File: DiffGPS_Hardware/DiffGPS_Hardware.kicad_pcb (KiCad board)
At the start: 2 copper layers, 87.6 x 72.1 mm, 17 parts, among them U1 Raspberry_Pi, U2 TSR_1-2450

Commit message: Finished Layout
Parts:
- removed the G*** at (116.8, 109.2)
- removed the G*** at (64.5, 73.2)
- added C1: 10uF, Capacitor_SMD:C_0603_1608Metric_Pad1.08x0.95mm_HandSolder, F.Cu at (63.4, 59.2)
- added C2: 10uF, Capacitor_SMD:C_0603_1608Metric_Pad1.08x0.95mm_HandSolder, F.Cu at (63.4, 61.4)
- added H4: MountingHole, MRDT_Drill_Holes:4_40_Hole_Corner, F.Cu at (50.9, 81.5)
- R1: value 1k -> 3k
- R3: value 120 -> 100
- U2: value TSR_1-2450 -> OKI; footprint MRDT_Devices:TSR_1-2433 -> MRDT_Devices:OKI_Horizontal
- moved G*** 3.97 mm to (111.3, 73.7)
- moved U2 2.05 mm to (68.6, 59.2)
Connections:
- net +12V renamed VCC
- net GPS_RX1 renamed D1
- net GPS_TX1 renamed D0
- net GPS_TX2 renamed D2
- A1 pad 10: unconnected-(A1-Pad10) -> A1
- A1 pad 11: unconnected-(A1-Pad11) -> A2
- A1 pad 12: unconnected-(A1-Pad12) -> A3
- A1 pad 13: unconnected-(A1-Pad13) -> A4
- A1 pad 14: unconnected-(A1-Pad14) -> A5
- A1 pad 18: unconnected-(A1-Pad18) -> D3
- A1 pad 19: unconnected-(A1-Pad19) -> D4
- A1 pad 20: unconnected-(A1-Pad20) -> D5
- A1 pad 21: unconnected-(A1-Pad21) -> D6
- A1 pad 22: unconnected-(A1-Pad22) -> D7
- A1 pad 23: GPS_RX2 -> D8
- A1 pad 24: unconnected-(A1-Pad24) -> D9
- A1 pad 25: unconnected-(A1-Pad25) -> D10
- A1 pad 26: unconnected-(A1-Pad26) -> D11
- A1 pad 27: unconnected-(A1-Pad27) -> D12
- A1 pad 28: unconnected-(A1-Pad28) -> D13
- A1 pad 9: unconnected-(A1-Pad9) -> A0
- U1 pad 12: unconnected-(U1-Pad12) -> D3
- U1 pad 13: unconnected-(U1-Pad13) -> D5
- U1 pad 15: unconnected-(U1-Pad15) -> D6
- U1 pad 16: GPS_RX2 -> D7
- U1 pad 19: unconnected-(U1-Pad19) -> D11
- U1 pad 21: unconnected-(U1-Pad21) -> D12
- U1 pad 22: unconnected-(U1-Pad22) -> D9
- U1 pad 23: unconnected-(U1-Pad23) -> D13
- U1 pad 24: unconnected-(U1-Pad24) -> D10
- U1 pad 26: unconnected-(U1-Pad26) -> D4
- U1 pad 29: unconnected-(U1-Pad29) -> A1
- U1 pad 3: unconnected-(U1-Pad3) -> A4
- U1 pad 31: unconnected-(U1-Pad31) -> A2
- U1 pad 32: unconnected-(U1-Pad32) -> A3
- U1 pad 5: unconnected-(U1-Pad5) -> A5
- U1 pad 7: unconnected-(U1-Pad7) -> A0
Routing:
- net D4: track 0.00 -> 86.1 mm, vias 0 -> 2
- net D11: track 0.00 -> 70.0 mm, vias 0 -> 2
- net D9: track 0.00 -> 68.2 mm
- net D3: track 0.00 -> 64.3 mm, vias 0 -> 2
- net D13: track 0.00 -> 62.7 mm
- net D12: track 0.00 -> 61.1 mm, vias 0 -> 2
- net GPS_RX2: track 60.8 -> 0.00 mm
- net D7: track 0.00 -> 60.1 mm
- net D10: track 0.00 -> 59.2 mm
- net D6: track 0.00 -> 55.9 mm
- net D5: track 0.00 -> 55.8 mm
- net A3: track 0.00 -> 39.6 mm, vias 0 -> 1
- net A2: track 0.00 -> 34.3 mm, vias 0 -> 1
- net A1: track 0.00 -> 30.5 mm, vias 0 -> 2
- net A0: track 0.00 -> 13.2 mm, vias 0 -> 2
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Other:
- board text added: "Differential GPS Breakout Board, Rev1 Mars Rover Design Team Missouri S&T, 2024 Will Grove, Natasha Cox"
- board text removed: "Differential GPS Breakout Board, Rev1 Mars Rover Design Team Missouri S&T, 2023 Grant Brinker"

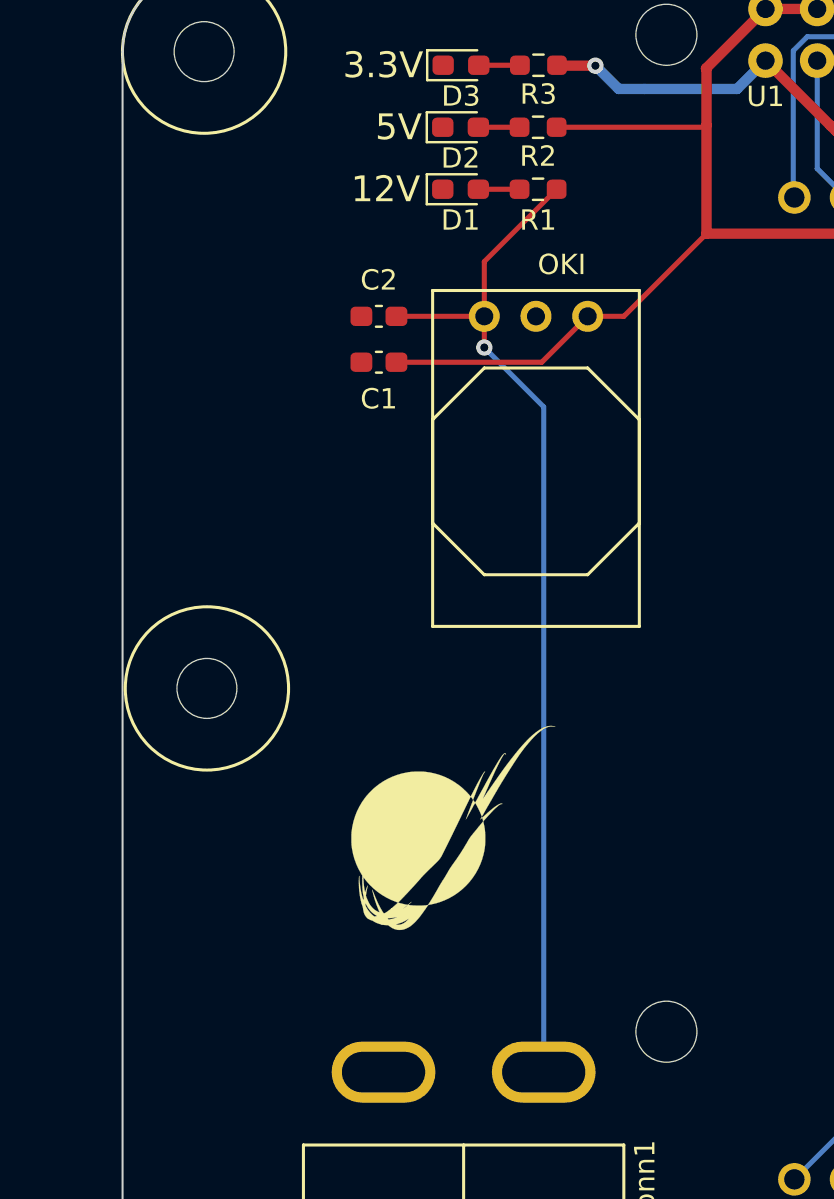
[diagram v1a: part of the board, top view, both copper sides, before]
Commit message: Fixed some stuff, changed trace width
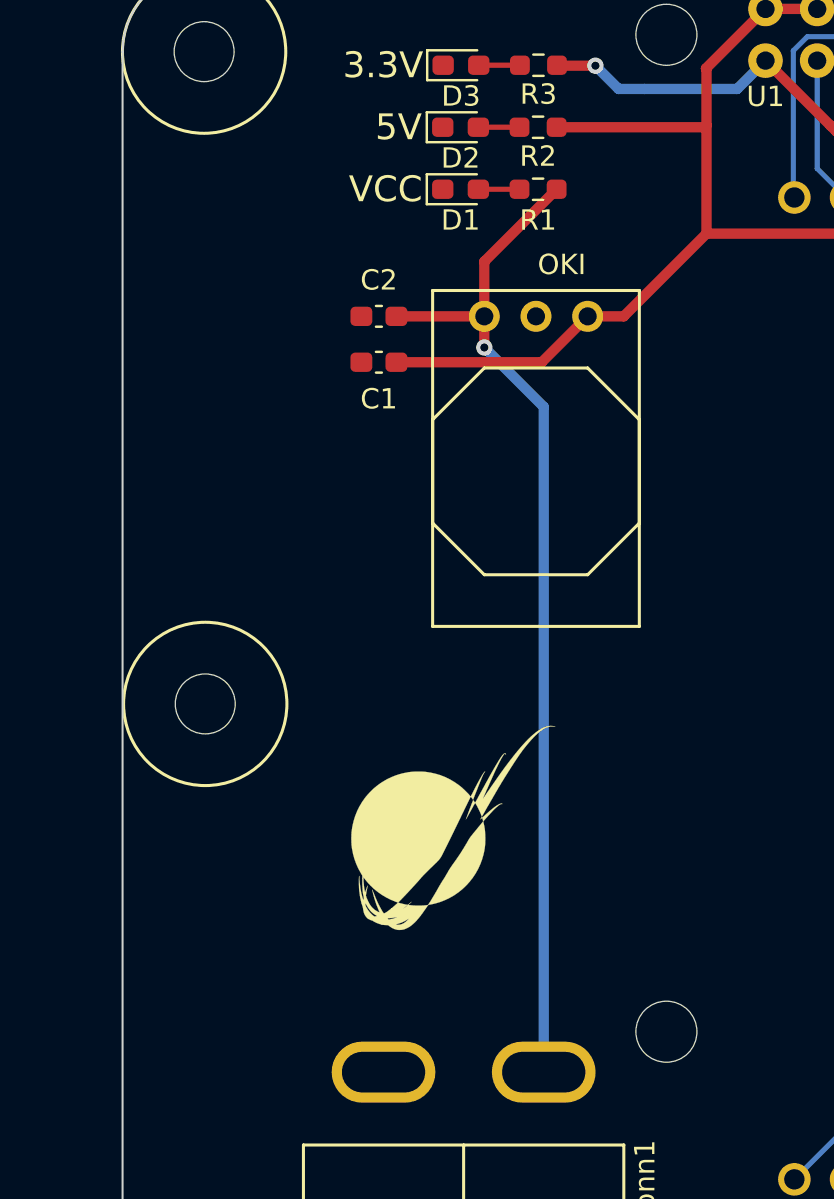
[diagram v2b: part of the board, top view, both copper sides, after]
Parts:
- moved H4 0.77 mm to (50.9, 82.2)
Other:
- board text added: "VCC"
- board text removed: "12V"
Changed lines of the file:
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@@
   )
   (footprint "MRDT_Drill_Holes:4_40_Hole_Corner" (layer "F.Cu")
-    (at 50.9383 81.47812)
+    (at 50.85588 82.24012)
     (property "Sheetfile" "DiffGPS_Hardware.kicad_sch")
     (property "Sheetname" "")
@@
     (effects (font (size 1 1) (thickness 0.15)) (justify left))
   )
-  (gr_text "12V" (at 63.7305 52.9355) (layer "F.SilkS")
+  (gr_text "VCC" (at 63.7305 52.9355) (layer "F.SilkS")
     (effects (font (size 1.27 1.27) (thickness 0.2032)))
   )
@@
   (segment (start 76.454 48.006) (end 75.184 48.006) (width 0.508) (layer "B.Cu") (net 2))
   (segment (start 116.84 51.308) (end 116.84 53.34) (width 0.508) (layer "B.Cu") (net 2))
-  (segment (start 72.136 49.8875) (end 79.3985 49.8875) (width 0.25) (layer "F.Cu") (net 5))
+  (segment (start 72.136 49.8875) (end 79.3985 49.8875) (width 0.508) (layer "F.Cu") (net 5))
   (segment (start 109.22 53.34) (end 107.442 55.118) (width 0.508) (layer "F.Cu") (net 5))
   (segment (start 79.3985 49.8875) (end 79.502 49.784) (width 0.25) (layer "F.Cu") (net 5))
   (segment (start 79.502 49.784) (end 79.502 47.028) (width 0.508) (layer "F.Cu") (net 5))
-  (segment (start 71.404 61.438) (end 73.66 59.182) (width 0.25) (layer "F.Cu") (net 5))
+  (segment (start 71.404 61.438) (end 73.66 59.182) (width 0.508) (layer "F.Cu") (net 5))
   (segment (start 79.474 47) (end 82.401 44.073) (width 0.508) (layer "F.Cu") (net 5))
   (segment (start 79.502 55.118) (end 79.502 49.784) (width 0.508) (layer "F.Cu") (net 5))
   (segment (start 107.442 55.118) (end 79.502 55.118) (width 0.508) (layer "F.Cu") (net 5))
-  (segment (start 75.438 59.182) (end 79.502 55.118) (width 0.25) (layer "F.Cu") (net 5))
+  (segment (start 75.438 59.182) (end 79.502 55.118) (width 0.508) (layer "F.Cu") (net 5))
   (segment (start 82.401 44.073) (end 84.941 44.073) (width 0.508) (layer "F.Cu") (net 5))
-  (segment (start 64.262 61.438) (end 71.404 61.438) (width 0.25) (layer "F.Cu") (net 5))
-  (segment (start 73.66 59.182) (end 75.438 59.182) (width 0.25) (layer "F.Cu") (net 5))
+  (segment (start 64.262 61.438) (end 71.404 61.438) (width 0.508) (layer "F.Cu") (net 5))
+  (segment (start 73.66 59.182) (end 75.438 59.182) (width 0.508) (layer "F.Cu") (net 5))
   (segment (start 79.502 47.028) (end 79.474 47) (width 0.508) (layer "F.Cu") (net 5))
   (segment (start 90.224 51.87) (end 90.17 51.816) (width 0.25) (layer "F.Cu") (net 8))
@@
   (segment (start 70.311 49.8875) (end 68.2885 49.8875) (width 0.254) (layer "F.Cu") (net 32))
   (segment (start 70.32975 46.8395) (end 68.30725 46.8395) (width 0.254) (layer "F.Cu") (net 33))
-  (segment (start 64.262 59.182) (end 68.58 59.182) (width 0.25) (layer "F.Cu") (net 34))
-  (segment (start 68.58 59.182) (end 68.58 60.7135) (width 0.25) (layer "F.Cu") (net 34))
-  (segment (start 68.58 56.4915) (end 68.58 59.182) (width 0.25) (layer "F.Cu") (net 34))
-  (segment (start 72.136 52.9355) (end 68.58 56.4915) (width 0.25) (layer "F.Cu") (net 34))
+  (segment (start 64.262 59.182) (end 68.58 59.182) (width 0.508) (layer "F.Cu") (net 34))
+  (segment (start 68.58 59.182) (end 68.58 60.7135) (width 0.508) (layer "F.Cu") (net 34))
+  (segment (start 68.58 56.4915) (end 68.58 59.182) (width 0.508) (layer "F.Cu") (net 34))
+  (segment (start 72.136 52.9355) (end 68.58 56.4915) (width 0.508) (layer "F.Cu") (net 34))
   (via (at 68.58 60.7135) (size 0.8) (drill 0.4) (layers "F.Cu" "B.Cu") (net 34))
-  (segment (start 71.501 63.6345) (end 71.501 96.3308) (width 0.25) (layer "B.Cu") (net 34))
-  (segment (start 68.58 60.7135) (end 71.501 63.6345) (width 0.25) (layer "B.Cu") (net 34))
+  (segment (start 71.501 63.6345) (end 71.501 96.3308) (width 0.508) (layer "B.Cu") (net 34))
+  (segment (start 68.58 60.7135) (end 71.501 63.6345) (width 0.508) (layer "B.Cu") (net 34))
   (zone (net 6) (net_name "GND") (layers "F&B.Cu") (hatch edge 0.508)
     (connect_pads yes (clearance 0.127))

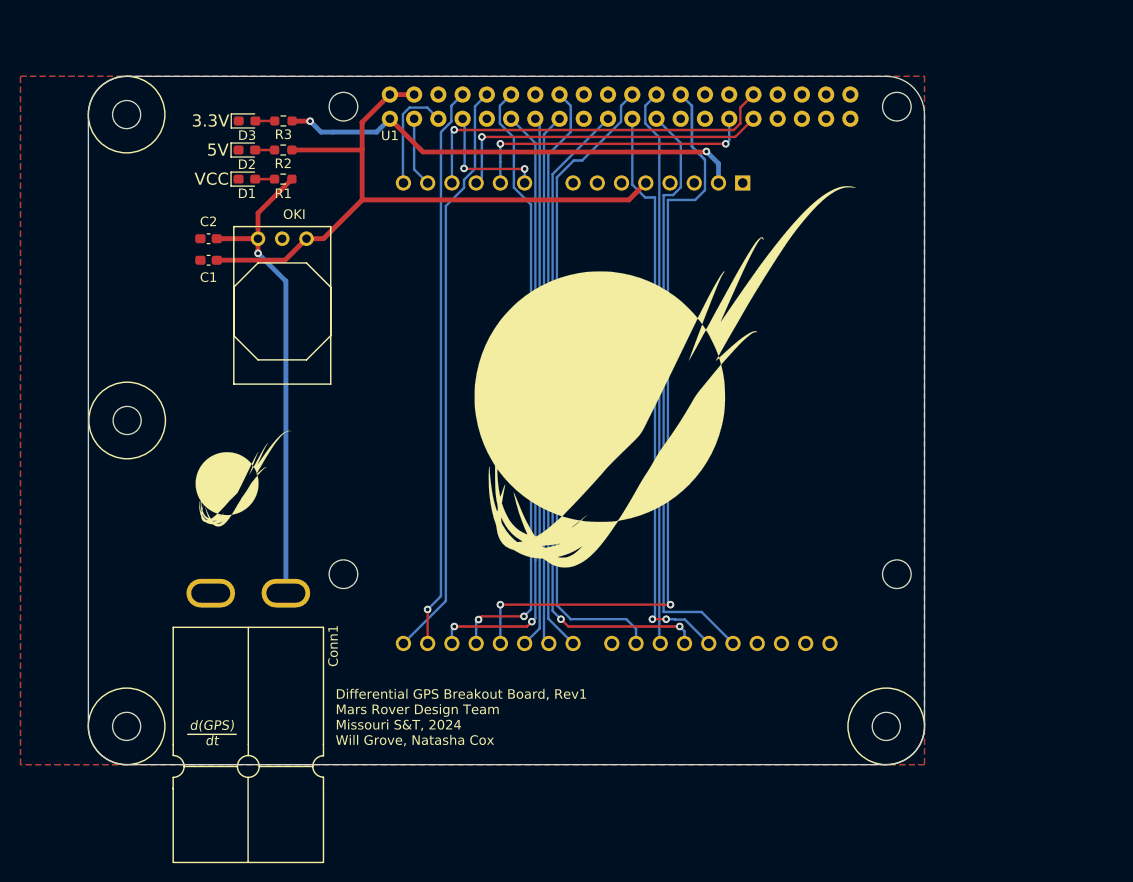
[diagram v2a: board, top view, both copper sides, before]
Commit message: Board Review - flipped arduino footprint
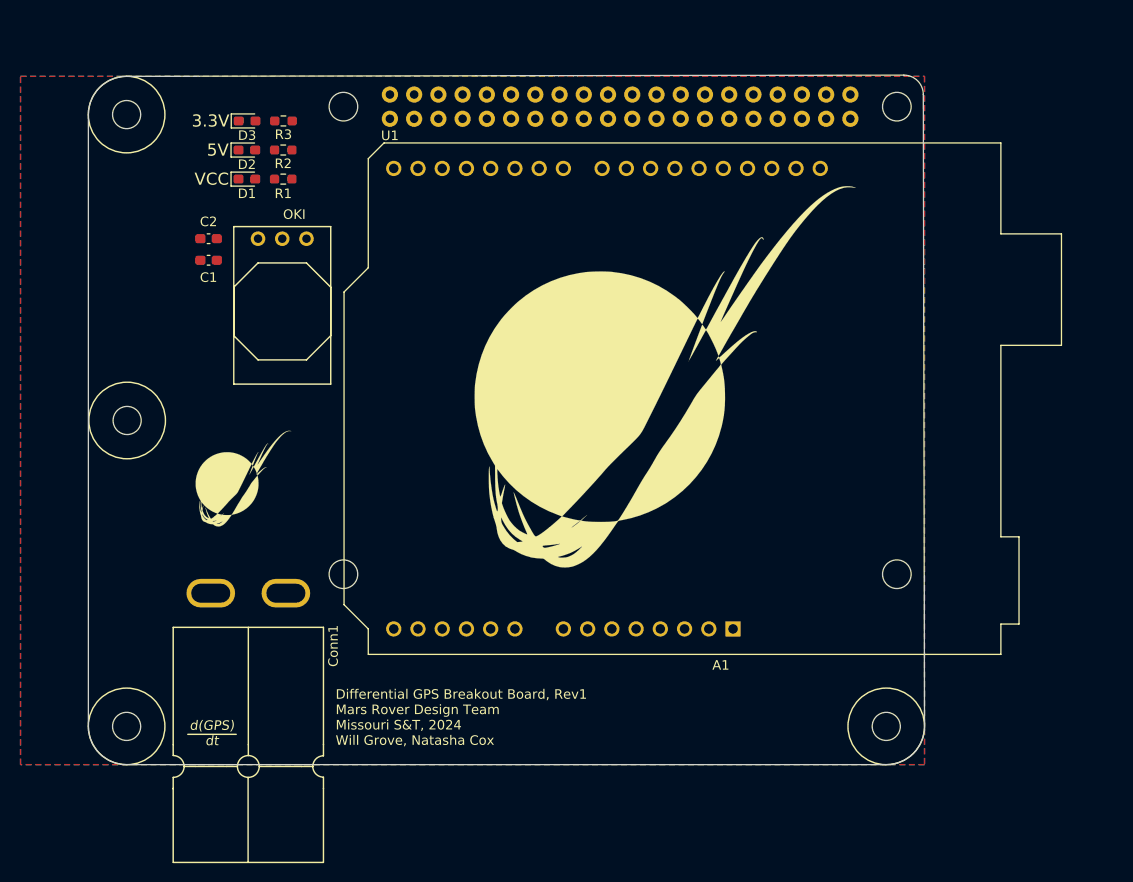
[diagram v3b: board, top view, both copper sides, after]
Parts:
- A1: moved to F.Cu
- moved A1 46.7 mm to (118.4, 100.1)
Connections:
- Conn1 pad 2: VCC -> (no net)
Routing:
- net D4: track 86.1 -> 0.00 mm, vias 2 -> 0
- net +5V: track 70.5 -> 0.00 mm
- net D11: track 70.0 -> 0.00 mm, vias 2 -> 0
- net D9: track 68.2 -> 0.00 mm
- net D3: track 64.3 -> 0.00 mm, vias 2 -> 0
- net D2: track 64.1 -> 0.00 mm, vias 2 -> 0
- net D13: track 62.7 -> 0.00 mm
- net D0: track 61.1 -> 0.00 mm
- net D12: track 61.1 -> 0.00 mm, vias 2 -> 0
- net D7: track 60.1 -> 0.00 mm
- net D10: track 59.2 -> 0.00 mm
- net D1: track 59.0 -> 0.00 mm, vias 1 -> 0
- net D6: track 55.9 -> 0.00 mm
- net D5: track 55.8 -> 0.00 mm
- net VCC: track 50.4 -> 0.00 mm, vias 1 -> 0
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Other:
- board size 87.6 x 72.1 mm -> 87.6 x 72.3 mm

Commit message: fixed edge cuts, started traces
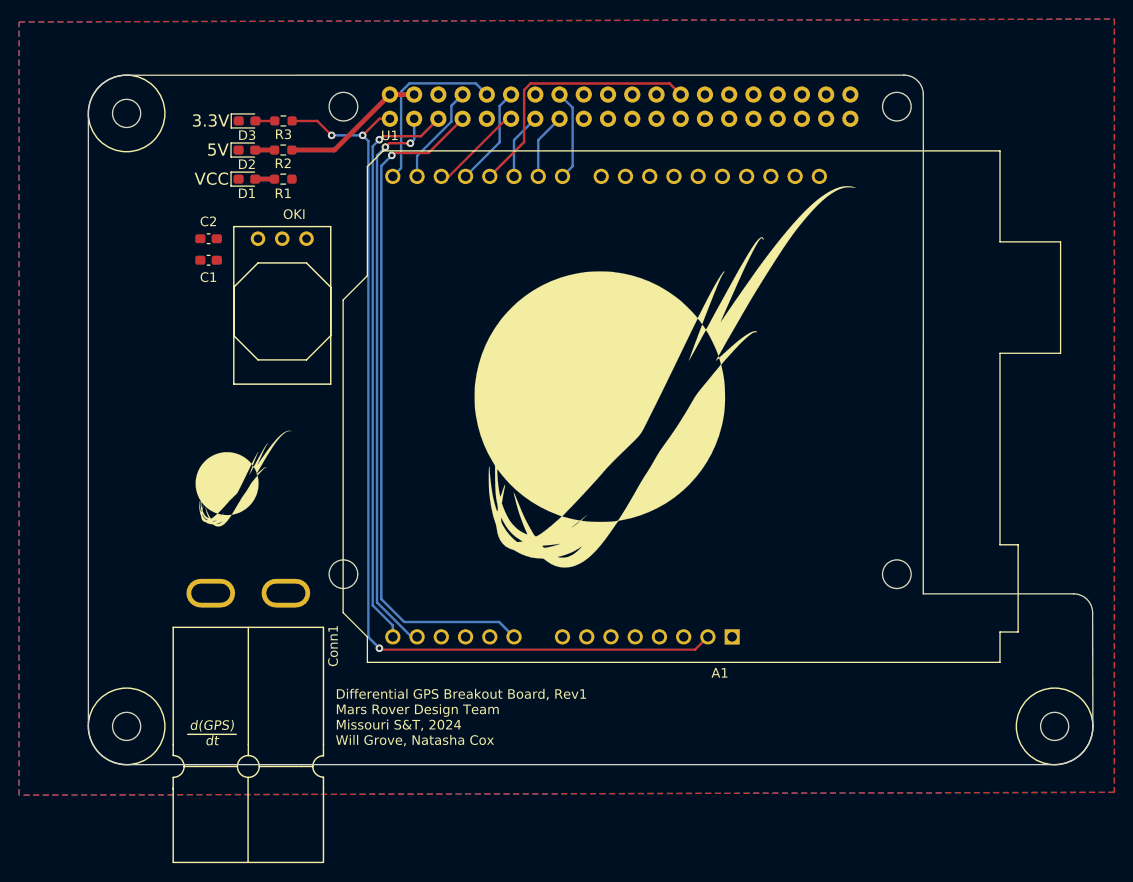
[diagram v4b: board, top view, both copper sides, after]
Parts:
- removed H4: MountingHole, MRDT_Drill_Holes:4_40_Hole_Corner
- moved H3 17.6 mm to (156.1, 114.3)
- moved A1 0.84 mm to (118.3, 100.9)
- moved H2 0.12 mm to (50.8, 42.0)
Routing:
- net +3V3: track 0.00 -> 101.1 mm, vias 0 -> 3
- net A0: track 0.00 -> 71.5 mm, vias 0 -> 1
- net A5: track 0.00 -> 60.4 mm, vias 0 -> 1
- net A4: track 0.00 -> 59.3 mm, vias 0 -> 2
- net D4: track 0.00 -> 27.7 mm
- net D0: track 0.00 -> 19.1 mm
- net +5V: track 0.00 -> 15.2 mm
- net D1: track 0.00 -> 10.6 mm
- net D3: track 0.00 -> 10.6 mm
- net D2: track 0.00 -> 9.81 mm
- net D7: track 0.00 -> 9.58 mm
- net D5: track 0.00 -> 6.96 mm
- net D6: track 0.00 -> 6.96 mm
- net Net-(D3-A): track 0.00 -> 2.02 mm
- net Net-(D2-A): track 0.00 -> 2.02 mm
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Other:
- board size 87.6 x 72.3 mm -> 105.3 x 72.3 mm
